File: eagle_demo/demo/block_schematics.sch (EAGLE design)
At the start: 0 parts

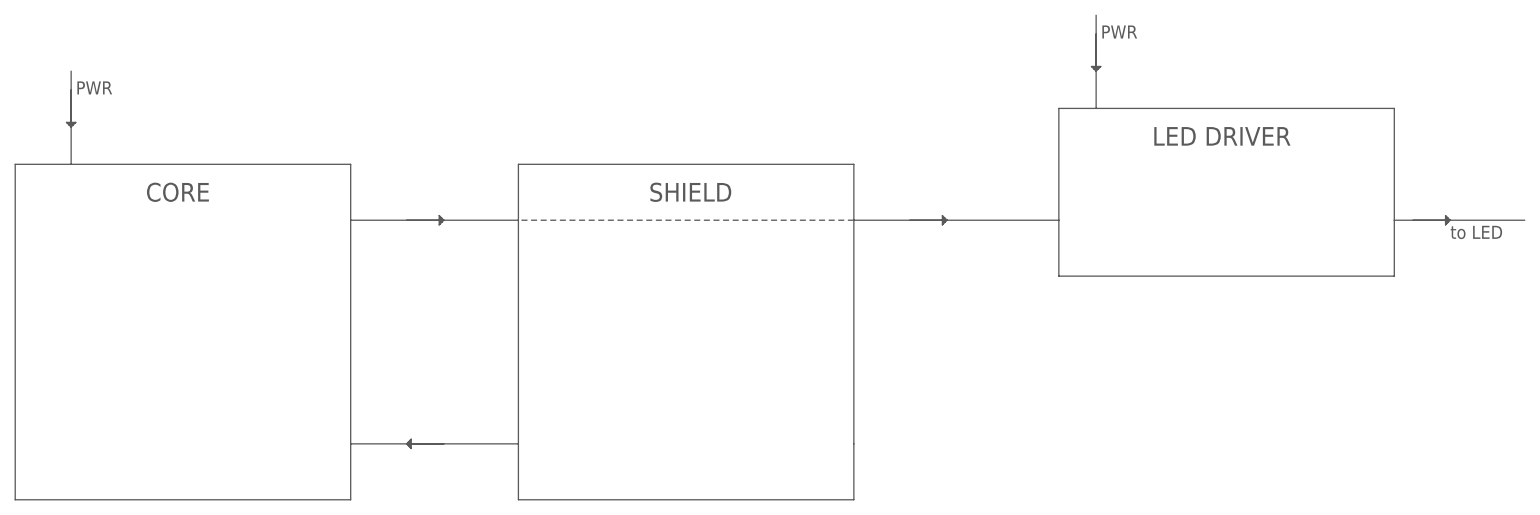
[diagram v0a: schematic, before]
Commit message: step 1.1 block diagram update
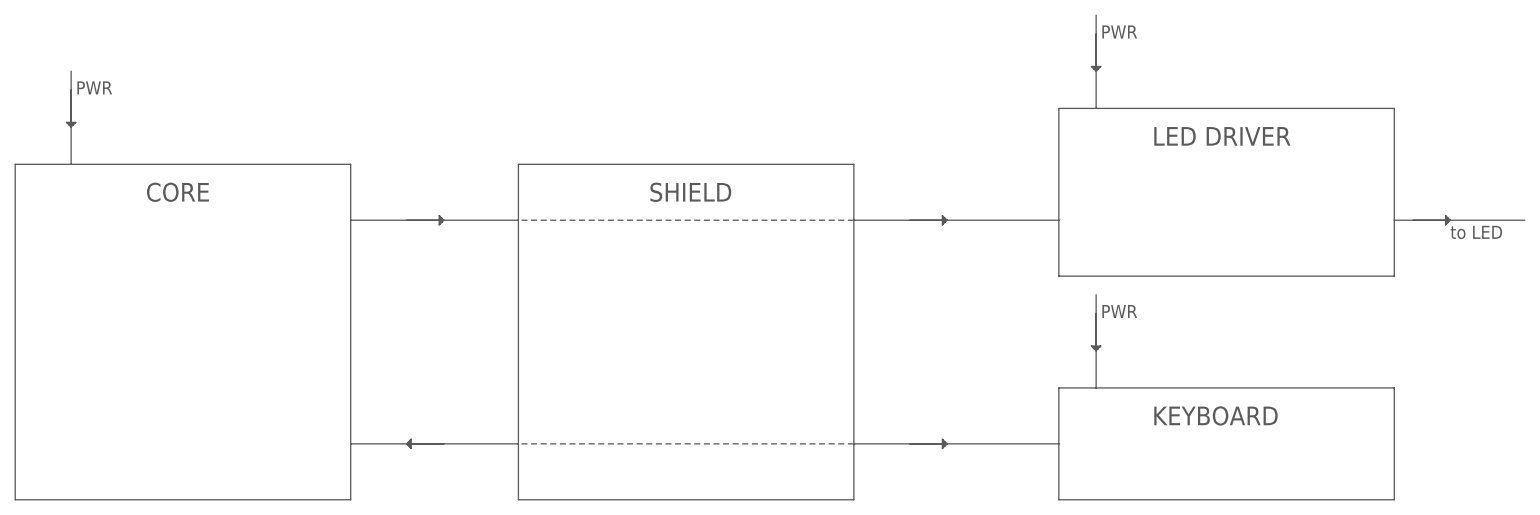
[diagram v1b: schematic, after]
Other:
- note added: "KEYBOARD"
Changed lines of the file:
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@@
 <part name="U$7" library="be_info" deviceset="ARROW_1" device=""/>
 <part name="U$8" library="be_info" deviceset="ARROW_1" device=""/>
+<part name="U$2" library="be_info" deviceset="ARROW_1" device=""/>
+<part name="U$6" library="be_info" deviceset="ARROW_1" device=""/>
 </parts>
 <sheets>
@@
 <text x="226.06" y="119.38" size="1.778" layer="97" font="fixed">to LED</text>
 <wire x1="144.78" y1="121.92" x2="99.06" y2="121.92" width="0.1524" layer="97" style="shortdash"/>
+<wire x1="172.72" y1="99.06" x2="177.8" y2="99.06" width="0.1524" layer="97"/>
+<wire x1="177.8" y1="99.06" x2="218.44" y2="99.06" width="0.1524" layer="97"/>
+<wire x1="218.44" y1="99.06" x2="218.44" y2="83.82" width="0.1524" layer="97"/>
+<wire x1="218.44" y1="83.82" x2="172.72" y2="83.82" width="0.1524" layer="97"/>
+<wire x1="172.72" y1="83.82" x2="172.72" y2="91.44" width="0.1524" layer="97"/>
+<text x="185.42" y="93.98" size="2.54" layer="97" font="fixed">KEYBOARD</text>
+<wire x1="172.72" y1="91.44" x2="172.72" y2="99.06" width="0.1524" layer="97"/>
+<wire x1="144.78" y1="91.44" x2="172.72" y2="91.44" width="0.1524" layer="97"/>
+<wire x1="177.8" y1="111.76" x2="177.8" y2="99.06" width="0.1524" layer="97"/>
+<text x="178.435" y="108.585" size="1.778" layer="97" font="fixed">PWR</text>
+<wire x1="144.78" y1="91.44" x2="99.06" y2="91.44" width="0.1524" layer="97" style="shortdash"/>
 </plain>
 <instances>
@@
 <instance part="U$7" gate="G$1" x="38.1" y="137.16" rot="R90"/>
 <instance part="U$8" gate="G$1" x="223.52" y="121.92" rot="R180"/>
+<instance part="U$2" gate="G$1" x="154.94" y="91.44" rot="R180"/>
+<instance part="U$6" gate="G$1" x="177.8" y="106.68" rot="R90"/>
 </instances>
 <busses>
